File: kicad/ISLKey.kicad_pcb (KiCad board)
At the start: 2 copper layers, 185.4 x 164.1 mm, 43 parts, among them J10 5-60V AC/DC IN, J11 12V OUT (lock/aux), J13 TTGO batt pads, J14 18650 pack, J3 Exit btn, J4 Door contact, J5 Tamper, J6 LOCK COM/NO/NC, J7 AUX COM/NO/NC, J8 Fire volt-free, J9 Fire link COM-Fire, K1 SRD-05VDC-SL-C, K2 SRD-05VDC-SL-C, M1 TTGO T-Display, Q1 PN2222A, Q2 PN2222A, U1 PC817, U3 TEN20-2412WIN, U4 TSR-1-2450

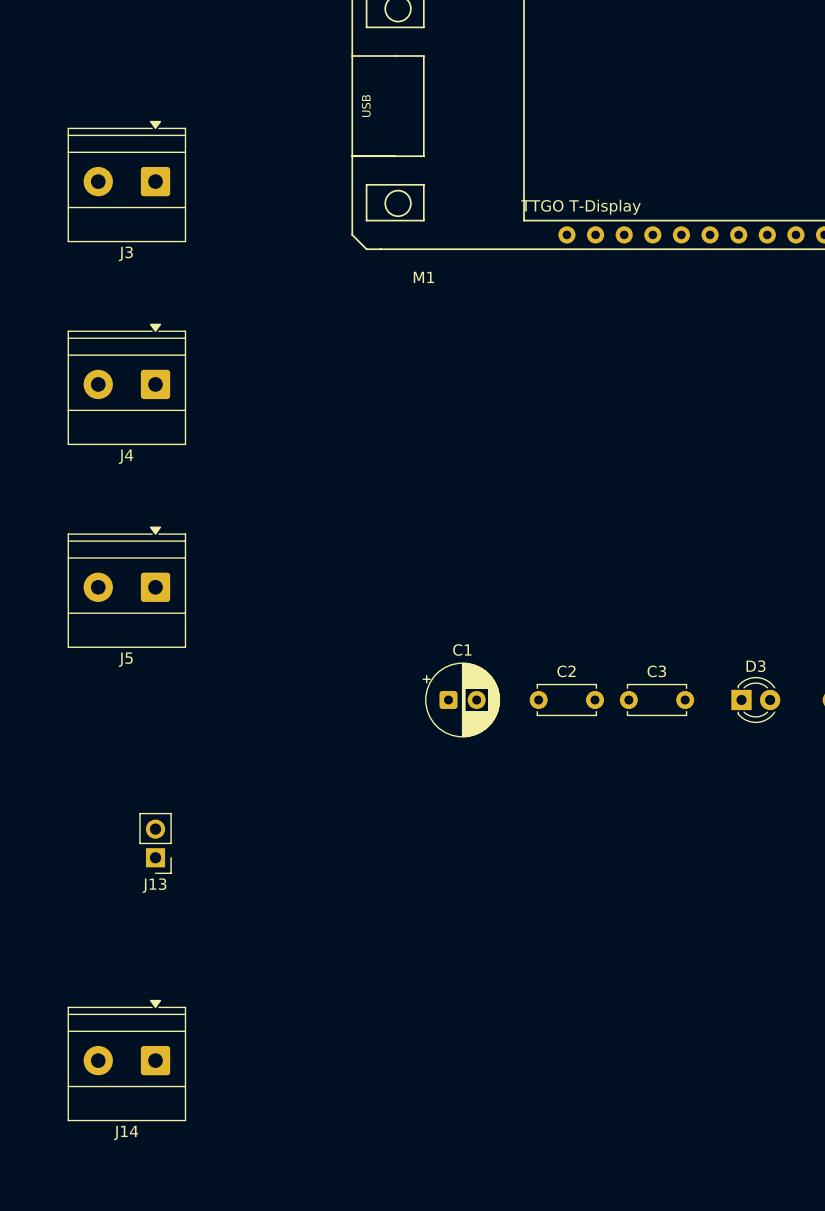
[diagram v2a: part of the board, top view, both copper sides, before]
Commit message: kicad: place battery pads (J13) between the TTGO header rows
The TTGO battery lead emerges between the two header rows, so centre the
2 solder pads (VBAT/GND_BAT) on M1's pad centroid rather than at the board
edge. J14 (18650-pack screw terminal) stays on the left edge; no on-board
holder (external holder via J14). DRC unchanged (no physical collisions).

Co-Authored-By: Claude Opus 4.8 <noreply@anthropic.com>
Claude-Session: https://claude.ai/code/session_01WaJbCVpNNC7xF4fkqWpjpA
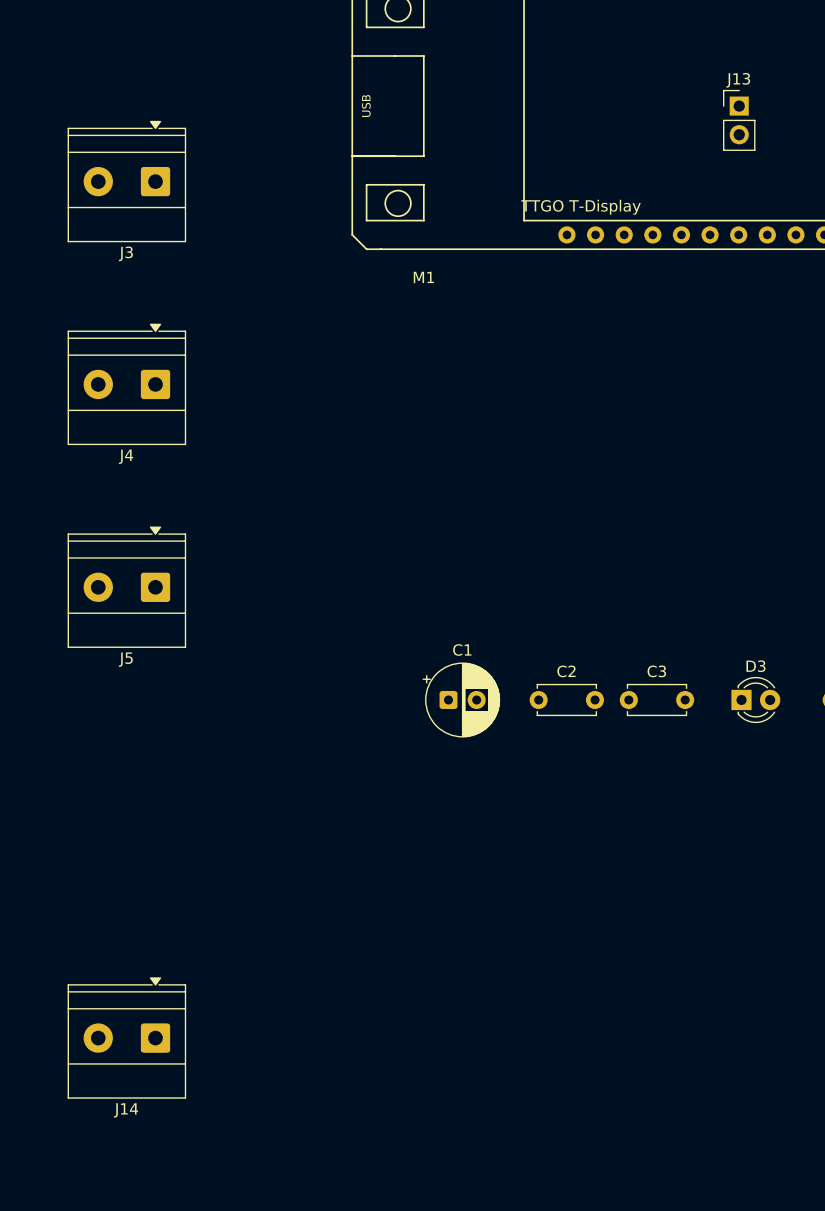
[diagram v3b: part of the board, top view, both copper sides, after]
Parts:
- moved J13 84.5 mm to (65.8, 17.3), turned to 0 degrees
- moved J14 2.00 mm to (14.0, 100.0)

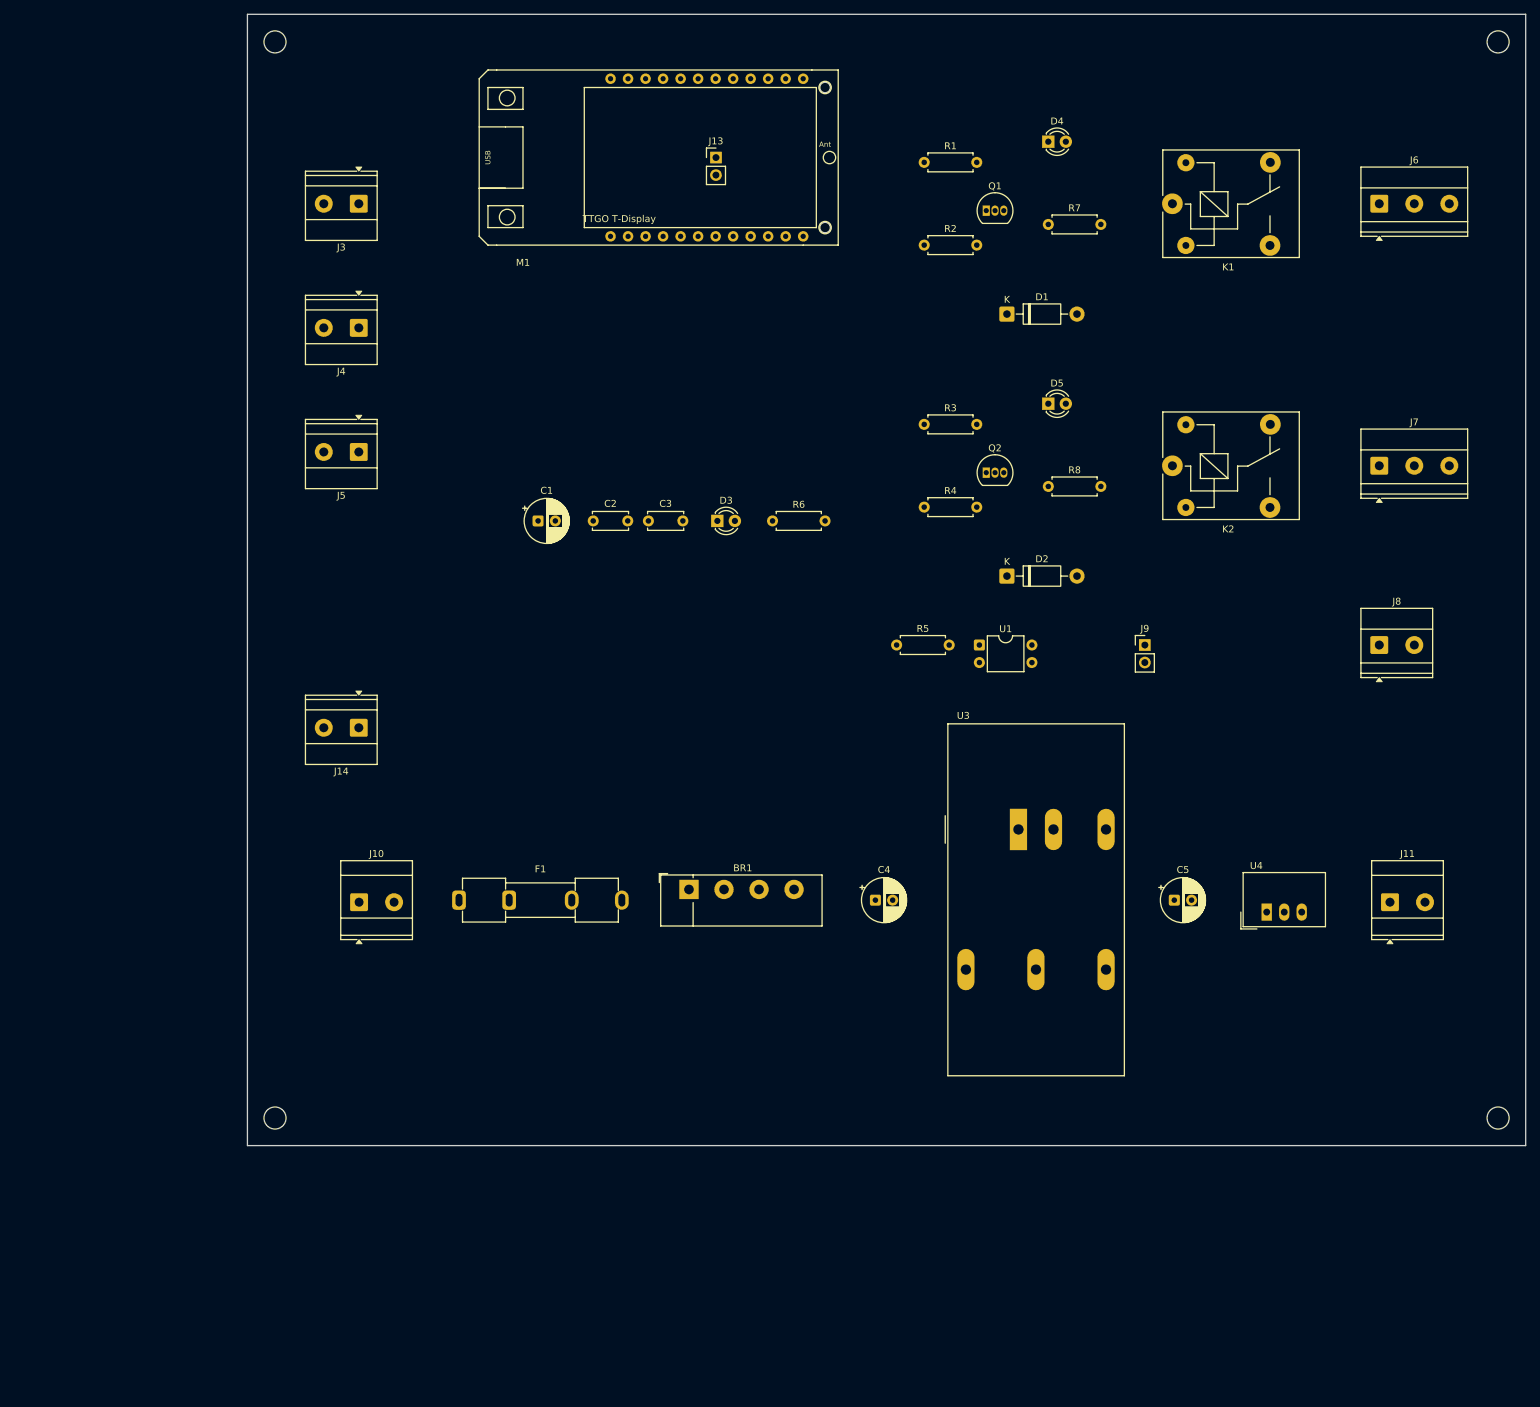
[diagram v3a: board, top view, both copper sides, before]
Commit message: kicad: add RTC (DS3231), on-board 2x18650 holders, and ground pour
- RTC: DS3231M (I2C on GPIO21/22 via the TTGO's onboard pull-ups),
  CR2032-backed (Keystone 3002) + 100nF. PWR_FLAGs on +3V3/RTC_VBAT.
- Battery: two Keystone 1042 1x18650 holders in parallel (BT1/BT2) on
  VBAT/GND_BAT, replacing the external-holder terminal (J14 removed).
- Ground plane: GND-filled zones on F.Cu and B.Cu (fill done on a reloaded
  board -- filling the freshly-built in-memory board segfaults pcbnew).

ERC 0/0, DRC no physical collisions (cosmetic silk/text-height only).
Board grows to ~219x200mm from the 18650 holders.

Co-Authored-By: Claude Opus 4.8 <noreply@anthropic.com>
Claude-Session: https://claude.ai/code/session_01WaJbCVpNNC7xF4fkqWpjpA
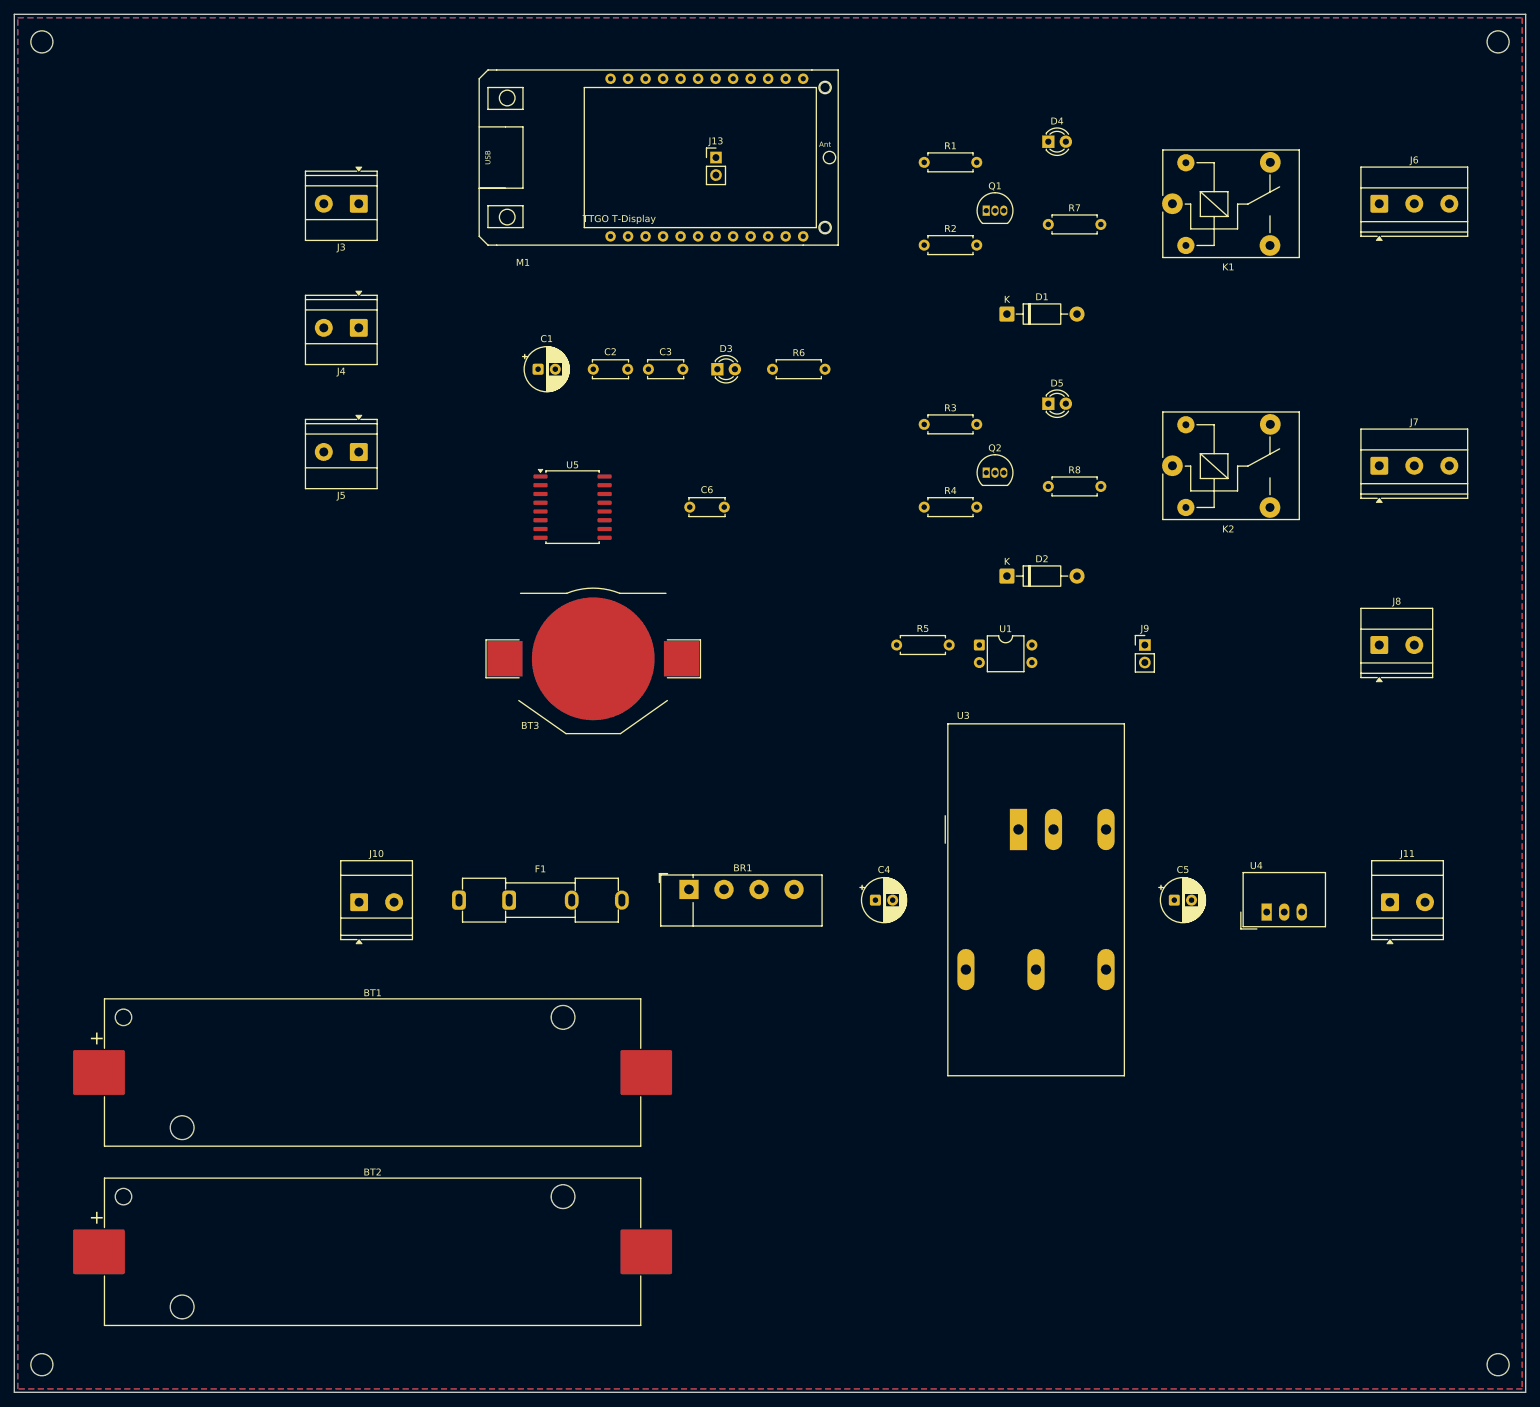
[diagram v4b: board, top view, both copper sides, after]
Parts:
- removed J14: 18650 pack, TerminalBlock_Phoenix_MKDS-1,5-2-5.08_1x02_P5.08mm_Horizontal
- added BT1: 18650, BatteryHolder_Keystone_1042_1x18650, F.Cu at (16.0, 150.0)
- added BT2: 18650, BatteryHolder_Keystone_1042_1x18650, F.Cu at (16.0, 176.0)
- added BT3: CR2032, BatteryHolder_Keystone_3002_1x2032, F.Cu at (48.0, 90.0)
- added C6: 100nF, C_Disc_D5.0mm_W2.5mm_P5.00mm, F.Cu at (62.0, 68.0)
- added U5: DS3231M, SOIC-16W_7.5x10.3mm_P1.27mm, F.Cu at (45.0, 68.0)
- moved H4 49.2 mm to (-32.0, 192.4)
- moved H3 35.8 mm to (179.2, 192.4)
- moved H1 33.8 mm to (-32.0, 0.53)
- moved C1 22.0 mm to (40.0, 48.0)
- moved C2 22.0 mm to (48.0, 48.0)
- moved C3 22.0 mm to (56.0, 48.0)
- moved D3 22.0 mm to (66.0, 48.0)
- moved R6 22.0 mm to (74.0, 48.0)
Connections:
- M1 pad 15: (no net) -> I2C_SDA
- M1 pad 16: (no net) -> I2C_SCL
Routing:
- added copper zone on B.Cu, net GND
- added copper zone on F.Cu, net GND
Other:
- board size 185.4 x 164.1 mm -> 219.2 x 199.9 mm

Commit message: kicad: pack the board tight (219x200 -> 141x156mm)
The old placement spaced parts by their SILK-TEXT bounding box (values like
"5-60V AC/DC IN" rendered ~53mm wide), leaving the board mostly empty. Fix:
- hide value silk; pack by the text-excluded body bbox GetBoundingBox(False,False)
- First-Fit-Decreasing-Height shelf pack (similar-height parts share a row)
- batteries broken out into their own block (78mm holders no longer inflate
  every shelf)

Board 140.9x155.7mm (was 219x200); circuit-only w/o the 18650s ~133x114.
Trade-off: this is size-optimised, grouped by height not signal flow -- final
routable arrangement is a GUI step. ERC 0, DRC no physical collisions.

Co-Authored-By: Claude Opus 4.8 <noreply@anthropic.com>
Claude-Session: https://claude.ai/code/session_01WaJbCVpNNC7xF4fkqWpjpA
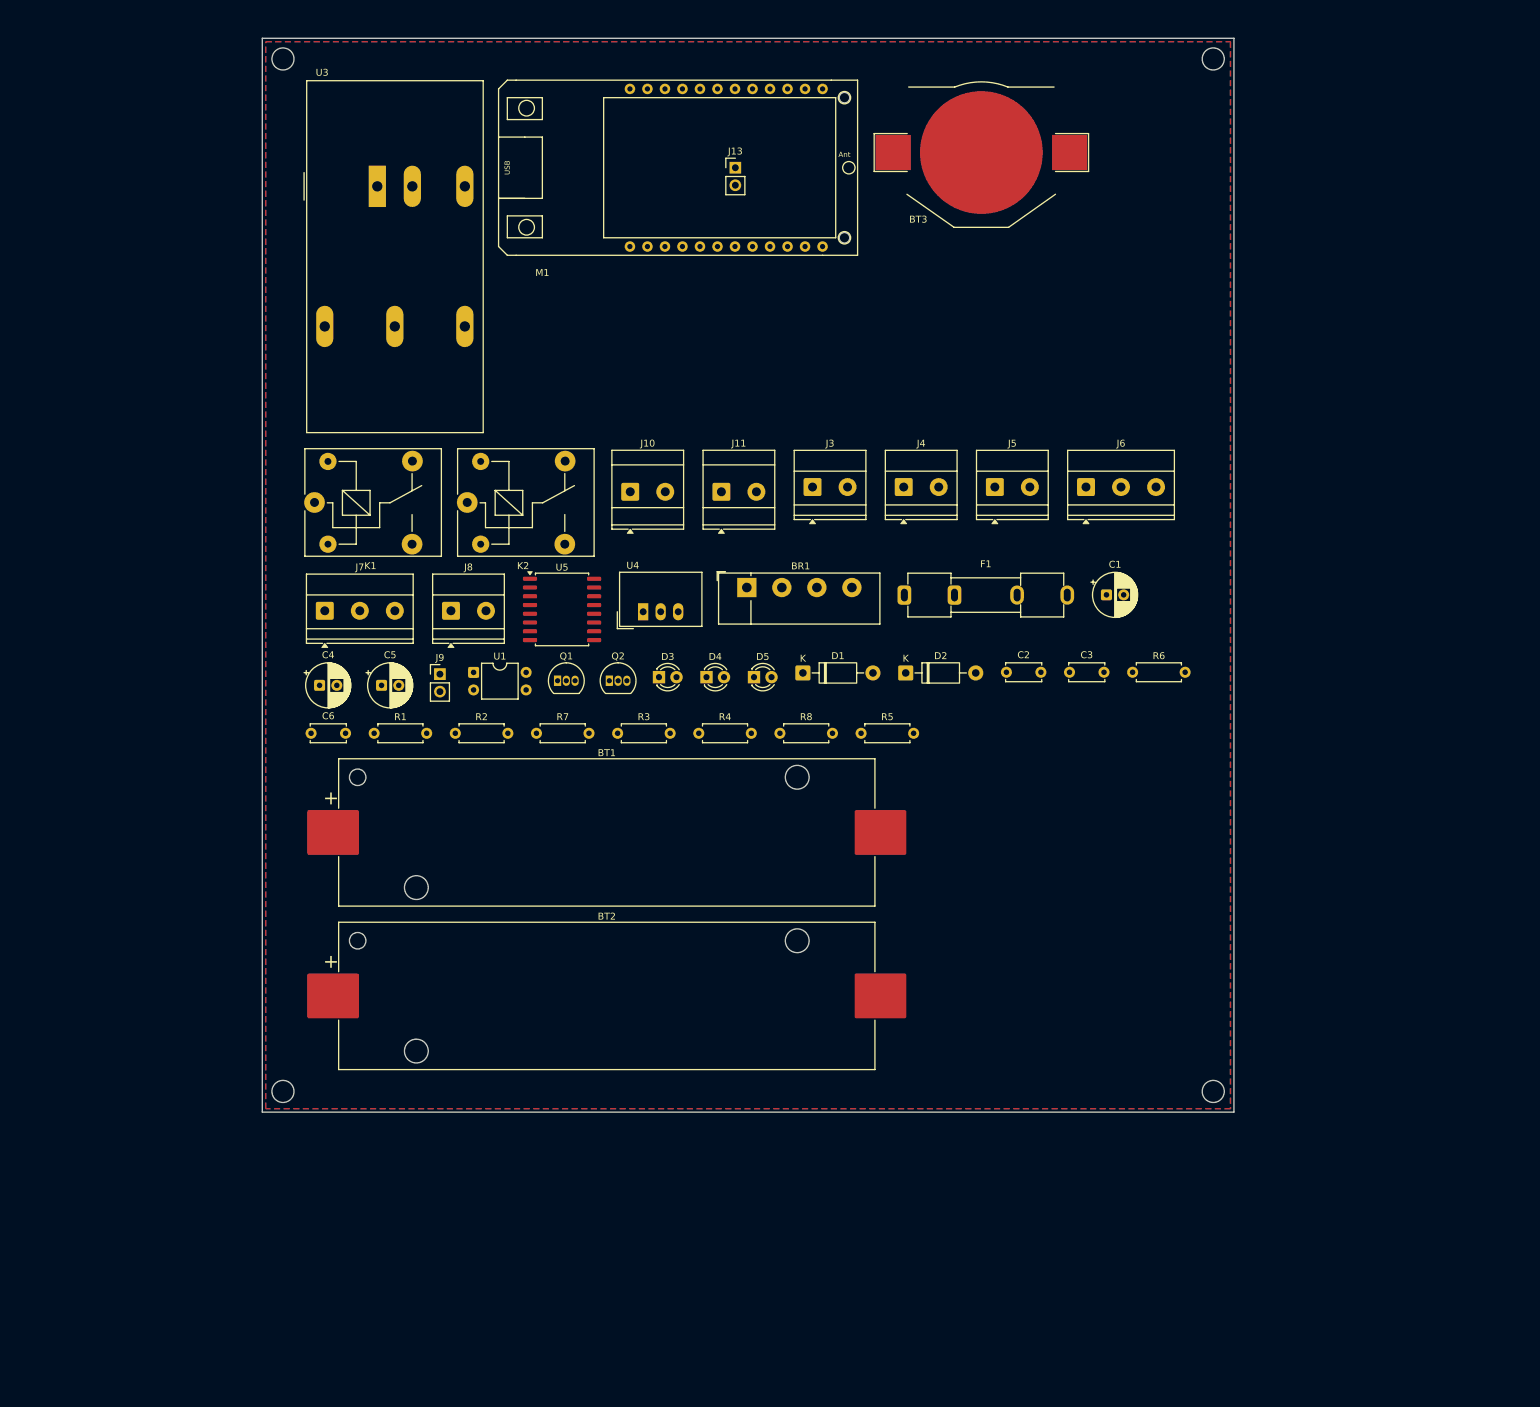
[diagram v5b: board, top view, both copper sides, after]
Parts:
- moved J7 154.4 mm to (9.06, 83.0)
- moved J8 134.7 mm to (27.4, 83.0)
- moved K1 131.8 mm to (7.58, 67.3)
- moved U3 131.7 mm to (16.7, 21.5)
- moved C5 119.1 mm to (17.3, 93.8)
- moved R1 115.0 mm to (16.2, 100.8)
- moved J11 113.8 mm to (66.6, 65.8)
- moved R7 104.7 mm to (39.8, 100.8)
- moved K2 102.4 mm to (29.7, 67.3)
- moved J9 102.3 mm to (25.8, 92.2)
- moved U4 100.4 mm to (55.2, 83.2)
- moved R2 98.2 mm to (28.0, 100.8)
- moved BT3 92.5 mm to (104.3, 16.6)
- moved J5 92.4 mm to (106.2, 65.1), turned to 0 degrees
- moved Q1 92.3 mm to (42.8, 93.2)
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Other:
- board size 219.2 x 199.9 mm -> 140.9 x 155.7 mm

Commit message: kicad: single 18650 backup cell (was 2x)
Drop to one Keystone 1042 18650 holder (BT1) on VBAT/GND_BAT -> 3.7V straight
to the TTGO LiPo input (no series/parallel question, ~3000mAh covers the 7h
backup target). Board 140.9x132mm.

Co-Authored-By: Claude Opus 4.8 <noreply@anthropic.com>
Claude-Session: https://claude.ai/code/session_01WaJbCVpNNC7xF4fkqWpjpA
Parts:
- removed BT2: 18650, BatteryHolder_Keystone_1042_1x18650
- moved H3 23.7 mm to (137.9, 129.0)
- moved H4 23.7 mm to (3.00, 129.0)
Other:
- board size 140.9 x 155.7 mm -> 140.9 x 132 mm
